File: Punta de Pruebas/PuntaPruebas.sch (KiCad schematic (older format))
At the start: 20 parts, among them P1 CONN_1, P2 CONN_1, SW1 Pulsador, SW2 Llave inversora, U1 40106

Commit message: Avances con la punta de pruebas
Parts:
- removed BZ1: Buzzer, symbol BUZZER_A
- removed C1: 1 uF, ~, symbol CP
- removed D1: 12V, ~, symbol ZENER
- removed D3: 4148, ~, symbol DIODE
- removed D4: AM, ~, symbol LED
- removed P1: CONN_1, ~, symbol CONN_1
- removed R1, R2, R3: 10K, symbol RESISTOR
- removed R4: 4M7, symbol RESISTOR
- removed R5, R6: 1K2, symbol RESISTOR
- removed RV1: 1M, ~, symbol POT
- removed SW1: Pulsador, ~, symbol SW_PUSH
- removed SW2: Llave inversora, symbol SW_SPDT
- added BZ1: BUZZER, symbol BUZZER
- added C1: 0.1 uF 50V, ~, symbol C
- added C2: CP, ~, symbol CP
- added D1: 1N4007, ~, symbol DIODE
- added D3: ZENER 12V, ~, symbol ZENER
- added D4: 4148, ~, symbol DIODE
- added D7: LED, ~, symbol LED
- added P1: CONN_2, ~, symbol CONN_2
- added P3: CONN_1, ~, symbol CONN_1
- added POT1: 1M, ~, symbol POT
- added PUSH1: Pulsador, ~, symbol SW_PUSH
- added R1, R2, R3: 10K, ~, symbol R
- added R4: 4M7, ~, symbol R
- added R5, R6: 1K2, ~, symbol R
- added SW1: Llave Inversora, symbol SW_SPDT
- D2: value 12V -> ZENER 12V
- D5: value RJ -> Rojo
- D6: value VD -> Verde
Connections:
- net labels added: Punta de señal, Toma de alimentación, VSS
- net labels removed: GND, Punta de Señal
- wire segments 40 -> 48

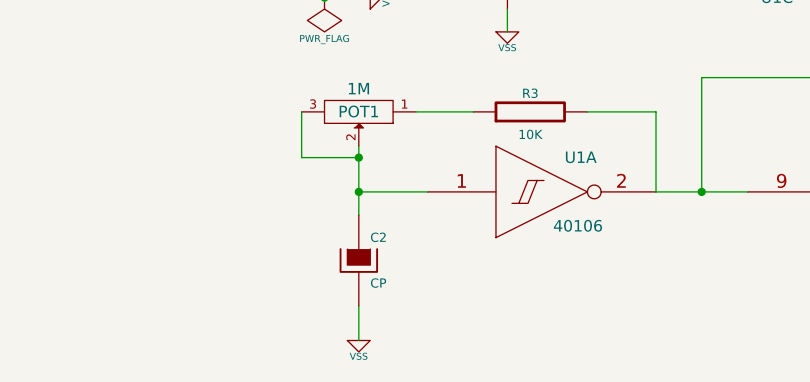
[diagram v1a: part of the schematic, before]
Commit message: mejora en el diseño del esquema y del pcb, agregado de modulos y librerias kicad para uso en todos los proyectos
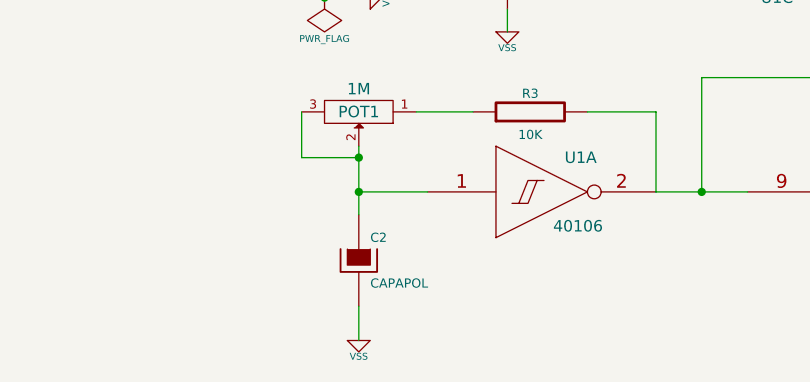
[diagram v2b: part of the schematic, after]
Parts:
- removed C2: CP, ~, symbol CP
- added C2: CAPAPOL, ~, symbol CAPAPOL
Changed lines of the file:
@@
 LIBS:valves
 LIBS:w_device
+LIBS:PuntaPruebas-cache
 EELAYER 27 0
 EELAYER END
@@
 $EndComp
 $Comp
-L CP C2
-U 1 1 52798923
-P 3650 4950
-F 0 "C2" H 3700 5050 40  0000 L CNN
-F 1 "CP" H 3700 4850 40  0000 L CNN
-F 2 "~" H 3750 4800 30  0000 C CNN
-F 3 "~" H 3650 4950 300 0000 C CNN
-	1    3650 4950
-	1    0    0    -1
-$EndComp
-$Comp
 L R R6
 U 1 1 52798B5A
@@
 Connection ~ 3500 3400
 Connection ~ 3500 3800
+$Comp
+L CAPAPOL C2
+U 1 1 52799D72
+P 3650 4950
+F 0 "C2" H 3700 5050 40  0000 L CNN
+F 1 "CAPAPOL" H 3700 4850 40  0000 L CNN
+F 2 "~" H 3750 4800 30  0000 C CNN
+F 3 "~" H 3650 4950 300 0000 C CNN
+	1    3650 4950
+	1    0    0    -1
+$EndComp
 $EndSCHEMATC

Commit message: PCB definitivo, incremento ancho de pista y mejoras en los archivos gerber
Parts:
- C2: value CAPAPOL -> 1 uF
- D7: value LED -> Amarillo
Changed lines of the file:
@@
 Sheet 1 1
 Title "Punta Lógica con generador de Pulsos"
-Date "6 nov 2013"
+Date "8 nov 2013"
 Rev "1.0"
 Comp "Nestor A. Scoccia"
@@
 $Comp
 L 40106 U1
-U 2 1 52798194
+U 1 1 52798194
 P 5650 2900
 F 0 "U1" H 5750 3050 50  0000 L CNN
@@
 F 2 "" H 5650 2900 60  0000 C CNN
 F 3 "" H 5650 2900 60  0000 C CNN
-	2    5650 2900
+	1    5650 2900
 	1    0    0    -1
 $EndComp
 $Comp
 L 40106 U1
-U 5 1 527981A3
+U 2 1 527981A3
 P 7350 2900
 F 0 "U1" H 7450 3050 50  0000 L CNN
@@
 F 2 "" H 7350 2900 60  0000 C CNN
 F 3 "" H 7350 2900 60  0000 C CNN
-	5    7350 2900
+	2    7350 2900
 	1    0    0    -1
 $EndComp
@@
 $Comp
 L 40106 U1
-U 1 1 527981BE
+U 6 1 527981BE
 P 4450 4650
 F 0 "U1" H 4550 4800 50  0000 L CNN
@@
 F 2 "" H 4450 4650 60  0000 C CNN
 F 3 "" H 4450 4650 60  0000 C CNN
-	1    4450 4650
+	6    4450 4650
 	1    0    0    -1
 $EndComp
 $Comp
 L 40106 U1
-U 4 1 527981CB
+U 5 1 527981CB
 P 5850 4650
 F 0 "U1" H 5950 4800 50  0000 L CNN
@@
 F 2 "" H 5850 4650 60  0000 C CNN
 F 3 "" H 5850 4650 60  0000 C CNN
-	4    5850 4650
+	5    5850 4650
 	1    0    0    -1
 $EndComp
@@
 P 7050 4650
 F 0 "D7" H 7050 4750 50  0000 C CNN
-F 1 "LED" H 7050 4550 50  0000 C CNN
+F 1 "Amarillo" H 7050 4550 50  0000 C CNN
 F 2 "~" H 7050 4650 60  0000 C CNN
 F 3 "~" H 7050 4650 60  0000 C CNN
@@
 P 3650 4950
 F 0 "C2" H 3700 5050 40  0000 L CNN
-F 1 "CAPAPOL" H 3700 4850 40  0000 L CNN
+F 1 "1 uF" H 3700 4850 40  0000 L CNN
 F 2 "~" H 3750 4800 30  0000 C CNN
 F 3 "~" H 3650 4950 300 0000 C CNN
